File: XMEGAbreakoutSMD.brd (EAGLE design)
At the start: 160 x 100 mm, 24 parts, among them IC1 XMEGA16A4

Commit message: fix to smd board
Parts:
- removed C3: 0.1uF, fab:C1206
- removed JUMPER2: 0, fab:R1206FAB
- moved R2 6.37 mm to (43.7, 38.1), turned to 270 degrees
- moved JP9 5.08 mm to (47.0, 21.6), turned to 0 degrees
- moved JP6 0.64 mm to (84.6, 60.1), turned to 180 degrees
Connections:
- net GND: no longer C3.2
- net RESET: no longer C3.1
- net VCC: now also JP6.2
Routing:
- net RESET: track 117.7 -> 32.7 mm
- net GND: track 246.7 -> 222.0 mm, vias 12 -> 10
- net VCC: track 70.0 -> 77.2 mm
- net DAT: track 43.9 -> 46.9 mm
- net VBUS: track 109.3 -> 107.6 mm
- net N$26: track 3.24 -> 2.13 mm

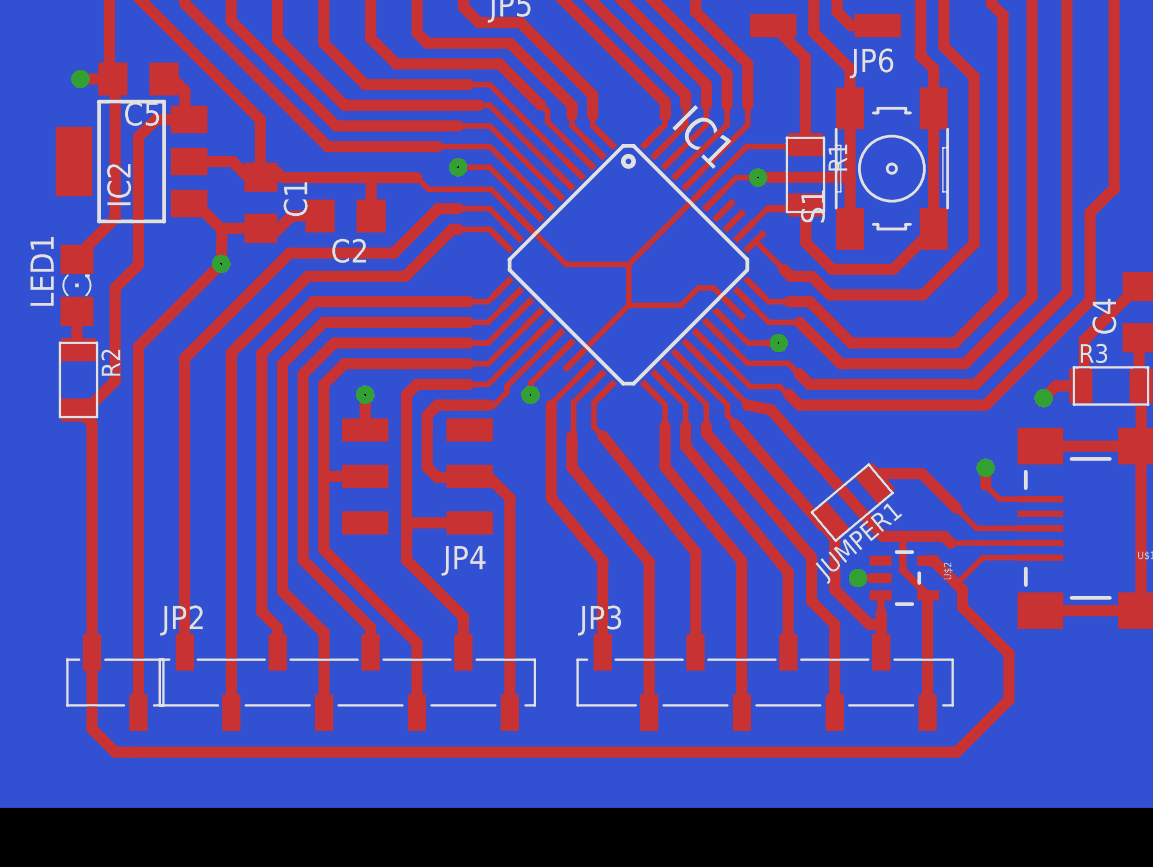
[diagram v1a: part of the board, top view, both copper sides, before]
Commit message: d+ and d- switched
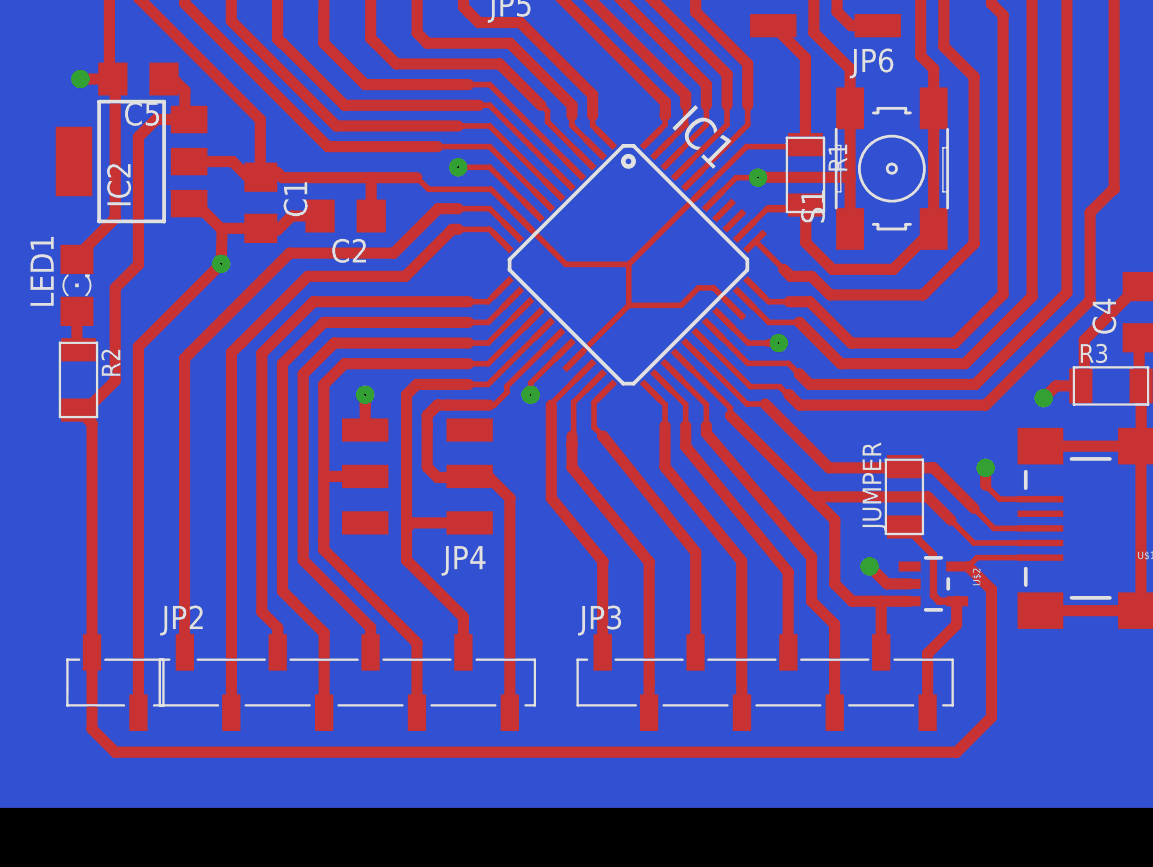
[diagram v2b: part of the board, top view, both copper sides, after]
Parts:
- removed JUMPER1: 0, fab:R1206FAB
- added JUMPER: 0Ohm, fab:R1206FAB
- moved U$2 1.62 mm to (90.5, 27.0)
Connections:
- net D+: now also IC1.27, JP3.1, U$2.4; no longer IC1.26, JP3.2, U$2.3
- net D-: now also IC1.26, JP3.2, U$2.3; no longer IC1.27, JP3.1, U$2.4
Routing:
- net D+: track 39.1 -> 35.7 mm
- net VBUS: track 107.6 -> 104.7 mm
- net D-: track 33.8 -> 36.5 mm

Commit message: final pngs
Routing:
- net GND: track 222.5 -> 228.3 mm, vias 10 -> 9
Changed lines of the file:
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@@
 <layer number="17" name="Pads" color="2" fill="1" visible="yes" active="yes"/>
 <layer number="18" name="Vias" color="2" fill="1" visible="yes" active="yes"/>
-<layer number="19" name="Unrouted" color="6" fill="1" visible="no" active="yes"/>
+<layer number="19" name="Unrouted" color="6" fill="1" visible="yes" active="yes"/>
 <layer number="20" name="Dimension" color="15" fill="1" visible="no" active="yes"/>
 <layer number="21" name="tPlace" color="7" fill="1" visible="no" active="yes"/>
@@
 <wire x1="51.5176125" y1="44.501325" x2="53.7401125" y2="42.42640625" width="0.6096" layer="16"/>
 <wire x1="53.7401125" y1="42.42640625" x2="59.396965625" y2="37.3352375" width="0.6096" layer="16"/>
-<wire x1="98.551890625" y1="37.81830625" x2="97.19080625" y2="37.81830625" width="0.6096" layer="1"/>
-<wire x1="97.19080625" y1="37.81830625" x2="96.52" y2="37.1475" width="0.6096" layer="1"/>
 <wire x1="96.341234375" y1="31.62404375" x2="94.10595625" y2="31.62404375" width="0.3048" layer="1"/>
 <wire x1="94.10595625" y1="31.62404375" x2="93.345" y2="32.385" width="0.3048" layer="1"/>
 <wire x1="93.345" y1="32.385" x2="93.345" y2="33.3375" width="0.6096" layer="1"/>
 <via x="93.345" y="33.3375" extent="1-16" drill="0.002540625" diameter="1.016"/>
-<via x="96.52" y="37.1475" extent="1-16" drill="0.002540625" diameter="1.016"/>
 <wire x1="96.52" y1="37.1475" x2="93.345" y2="37.1475" width="0.6096" layer="16"/>
 <wire x1="93.345" y1="37.1475" x2="93.07655" y2="37.1475" width="0.6096" layer="16"/>
@@
 <wire x1="83.947" y1="61.595" x2="82.931" y2="62.611" width="0.6096" layer="1"/>
 <wire x1="82.931" y1="62.611" x2="81.7245" y2="62.611" width="0.6096" layer="1"/>
-<wire x1="43.46418125" y1="50.095684375" x2="43.815" y2="52.2039375" width="0" layer="19" extent="1-16"/>
 <wire x1="89.1874" y1="26.9875" x2="87.9475" y2="26.9875" width="0.6096" layer="1"/>
 <wire x1="87.9475" y1="26.9875" x2="86.995" y2="27.94" width="0.6096" layer="1"/>
+<wire x1="98.551890625" y1="37.81830625" x2="95.92080625" y2="37.81830625" width="0.6096" layer="1"/>
+<wire x1="95.92080625" y1="37.81830625" x2="93.345" y2="35.2425" width="0.6096" layer="1"/>
+<wire x1="93.345" y1="35.2425" x2="93.345" y2="33.3375" width="0.6096" layer="1"/>
+<wire x1="43.815" y1="52.2039375" x2="43.46418125" y2="50.095684375" width="0" layer="19" extent="1-16"/>
 </signal>
 <signal name="VCC">
